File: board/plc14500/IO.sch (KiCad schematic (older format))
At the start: 70 parts, among them U1 74HC14, U2 4051, U3 74HC14, U4 NE555, U5 4099, U6 Arduino Nano

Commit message: Nano board rev-a prod ready
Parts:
- removed R22: 0R, Resistor_THT:R_Axial_DIN0204_L3.6mm_D1.6mm_P7.62mm_Horizontal, symbol Device:R
- D1, D10, D11, D12, D13, D14, D15, D16, D17, D2, D3, D4, D5, D6, D7, D8, D9: value LED 5MM Red -> LED 3MM Red
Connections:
- net +5V: now also U6.27 (+5V)
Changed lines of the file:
@@
 P 7900 2075
 F 0 "D9" H 7925 2150 45  0000 L CNN
-F 1 "LED 5MM Red" H 7978 2036 45  0001 L CNN
+F 1 "LED 3MM Red" H 7978 2036 45  0001 L CNN
 F 2 "plc14500:LED_3MM" V 7700 2075 20  0001 C CNN
 F 3 "" H 7900 2075 50  0001 C CNN
@@
 P 8075 2075
 F 0 "D10" H 8100 2150 45  0000 L CNN
-F 1 "LED 5MM Red" H 8153 2036 45  0001 L CNN
+F 1 "LED 3MM Red" H 8153 2036 45  0001 L CNN
 F 2 "plc14500:LED_3MM" V 7875 2075 20  0001 C CNN
 F 3 "" H 8075 2075 50  0001 C CNN
@@
 P 8250 2075
 F 0 "D11" H 8275 2150 45  0000 L CNN
-F 1 "LED 5MM Red" H 8328 2036 45  0001 L CNN
+F 1 "LED 3MM Red" H 8328 2036 45  0001 L CNN
 F 2 "plc14500:LED_3MM" V 8050 2075 20  0001 C CNN
 F 3 "" H 8250 2075 50  0001 C CNN
@@
 P 8425 2075
 F 0 "D12" H 8450 2150 45  0000 L CNN
-F 1 "LED 5MM Red" H 8503 2036 45  0001 L CNN
+F 1 "LED 3MM Red" H 8503 2036 45  0001 L CNN
 F 2 "plc14500:LED_3MM" V 8225 2075 20  0001 C CNN
 F 3 "" H 8425 2075 50  0001 C CNN
@@
 P 8600 2075
 F 0 "D13" H 8625 2150 45  0000 L CNN
-F 1 "LED 5MM Red" H 8678 2036 45  0001 L CNN
+F 1 "LED 3MM Red" H 8678 2036 45  0001 L CNN
 F 2 "plc14500:LED_3MM" V 8400 2075 20  0001 C CNN
 F 3 "" H 8600 2075 50  0001 C CNN
@@
 P 8775 2075
 F 0 "D14" H 8800 2150 45  0000 L CNN
-F 1 "LED 5MM Red" H 8853 2036 45  0001 L CNN
+F 1 "LED 3MM Red" H 8853 2036 45  0001 L CNN
 F 2 "plc14500:LED_3MM" V 8575 2075 20  0001 C CNN
 F 3 "" H 8775 2075 50  0001 C CNN
@@
 P 8950 2075
 F 0 "D15" H 8975 2150 45  0000 L CNN
-F 1 "LED 5MM Red" H 9028 2036 45  0001 L CNN
+F 1 "LED 3MM Red" H 9028 2036 45  0001 L CNN
 F 2 "plc14500:LED_3MM" V 8750 2075 20  0001 C CNN
 F 3 "" H 8950 2075 50  0001 C CNN
@@
 P 9125 2075
 F 0 "D16" H 9150 2150 45  0000 L CNN
-F 1 "LED 5MM Red" H 9203 2036 45  0001 L CNN
+F 1 "LED 3MM Red" H 9203 2036 45  0001 L CNN
 F 2 "plc14500:LED_3MM" V 8925 2075 20  0001 C CNN
 F 3 "" H 9125 2075 50  0001 C CNN
@@
 P 2250 1875
 F 0 "D1" V 2300 1900 45  0000 L CNN
-F 1 "LED 5MM Red" H 2328 1836 45  0001 L CNN
+F 1 "LED 3MM Red" H 2328 1836 45  0001 L CNN
 F 2 "plc14500:LED_3MM" V 2050 1875 20  0001 C CNN
 F 3 "" H 2250 1875 50  0001 C CNN
@@
 P 6125 6800
 F 0 "D8" H 6150 6875 45  0000 L CNN
-F 1 "LED 5MM Red" H 6203 6761 45  0001 L CNN
+F 1 "LED 3MM Red" H 6203 6761 45  0001 L CNN
 F 2 "plc14500:LED_3MM" V 5925 6800 20  0001 C CNN
 F 3 "" H 6125 6800 50  0001 C CNN
@@
 P 9675 5150
 F 0 "D17" H 9700 5225 45  0000 L CNN
-F 1 "LED 5MM Red" H 9753 5111 45  0001 L CNN
+F 1 "LED 3MM Red" H 9753 5111 45  0001 L CNN
 F 2 "plc14500:LED_3MM" V 9475 5150 20  0001 C CNN
 F 3 "" H 9675 5150 50  0001 C CNN
@@
 P 2250 3500
 F 0 "D2" V 2300 3525 45  0000 L CNN
-F 1 "LED 5MM Red" H 2328 3461 45  0001 L CNN
+F 1 "LED 3MM Red" H 2328 3461 45  0001 L CNN
 F 2 "plc14500:LED_3MM" V 2050 3500 20  0001 C CNN
 F 3 "" H 2250 3500 50  0001 C CNN
@@
 P 2250 4975
 F 0 "D3" V 2300 5000 45  0000 L CNN
-F 1 "LED 5MM Red" H 2328 4936 45  0001 L CNN
+F 1 "LED 3MM Red" H 2328 4936 45  0001 L CNN
 F 2 "plc14500:LED_3MM" V 2050 4975 20  0001 C CNN
 F 3 "" H 2250 4975 50  0001 C CNN
@@
 P 2250 6450
 F 0 "D4" V 2300 6475 45  0000 L CNN
-F 1 "LED 5MM Red" H 2328 6411 45  0001 L CNN
+F 1 "LED 3MM Red" H 2328 6411 45  0001 L CNN
 F 2 "plc14500:LED_3MM" V 2050 6450 20  0001 C CNN
 F 3 "" H 2250 6450 50  0001 C CNN
@@
 P 4775 2025
 F 0 "D5" V 4825 2050 45  0000 L CNN
-F 1 "LED 5MM Red" H 4853 1986 45  0001 L CNN
+F 1 "LED 3MM Red" H 4853 1986 45  0001 L CNN
 F 2 "plc14500:LED_3MM" V 4575 2025 20  0001 C CNN
 F 3 "" H 4775 2025 50  0001 C CNN
@@
 P 4775 3500
 F 0 "D6" V 4825 3525 45  0000 L CNN
-F 1 "LED 5MM Red" H 4853 3461 45  0001 L CNN
+F 1 "LED 3MM Red" H 4853 3461 45  0001 L CNN
 F 2 "plc14500:LED_3MM" V 4575 3500 20  0001 C CNN
 F 3 "" H 4775 3500 50  0001 C CNN
@@
 P 4775 5000
 F 0 "D7" V 4825 5025 45  0000 L CNN
-F 1 "LED 5MM Red" H 4853 4961 45  0001 L CNN
+F 1 "LED 3MM Red" H 4853 4961 45  0001 L CNN
 F 2 "plc14500:LED_3MM" V 4575 5000 20  0001 C CNN
 F 3 "" H 4775 5000 50  0001 C CNN
@@
 Wire Wire Line
 	6900 1400 7075 1400
-$Comp
-L Device:R R22
-U 1 1 68128BF1
-P 8600 3300
-F 0 "R22" V 8700 3300 50  0000 R CNN
-F 1 "0R" V 8500 3300 50  0000 R CNN
-F 2 "Resistor_THT:R_Axial_DIN0204_L3.6mm_D1.6mm_P7.62mm_Horizontal" V 8530 3300 50  0001 C CNN
-F 3 "~" H 8600 3300 50  0001 C CNN
-F 4 "0.01" H 8600 3300 50  0001 C CNN "Price"
-	1    8600 3300
-	0    1    1    0
-$EndComp
 Wire Wire Line
 	8300 3400 8300 3300
-Wire Wire Line
-	8300 3300 8450 3300
-Wire Wire Line
-	8750 3300 8925 3300
 Wire Wire Line
 	8925 3300 8925 3225
@@
 	1    0    0    -1
 $EndComp
+Wire Wire Line
+	8300 3300 8925 3300
 Wire Bus Line
 	6825 1750 6825 2000

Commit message: Update board 3d models
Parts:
- RV1: footprint Potentiometer_THT:Potentiometer_ACP_CA9-H5_Horizontal -> plc14500:HORIZONTAL_POT
- S1, S10, S11, S15, S2, S3, S4, S9: footprint Button_Switch_THT:SW_Tactile_Straight_KSA0Axx1LFTR -> plc14500:SW_Tactile_THT
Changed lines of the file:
@@
 F 0 "S1" V 1075 1500 50  0000 R CNN
 F 1 "Push Button" V 855 1277 50  0001 R CNN
-F 2 "Button_Switch_THT:SW_Tactile_Straight_KSA0Axx1LFTR" H 900 1525 50  0001 C CNN
+F 2 "plc14500:SW_Tactile_THT" H 900 1525 50  0001 C CNN
 F 3 "~" H 900 1525 50  0001 C CNN
 F 4 "0.01" H 900 1325 50  0001 C CNN "Price"
@@
 F 0 "RV1" H 5056 5821 50  0000 R CNN
 F 1 "10K" H 5056 5730 50  0000 R CNN
-F 2 "Potentiometer_THT:Potentiometer_ACP_CA9-H5_Horizontal" H 5125 5775 50  0001 C CNN
+F 2 "plc14500:HORIZONTAL_POT" H 5125 5775 50  0001 C CNN
 F 3 "~" H 5125 5775 50  0001 C CNN
 F 4 "https://www.aliexpress.com/item/1005002935520232.html?spm=a2g0o.productlist.0.0.7a175d89PQda4t&algo_pvid=cfb4e09e-1f4a-43cf-8ff1-6fc20f5cfef2&algo_exp_id=cfb4e09e-1f4a-43cf-8ff1-6fc20f5cfef2-21&pdp_ext_f=%7B%22sku_id%22%3A%2212000022869515902%22%7D&pdp_npi=2%40dis%21EUR%211.49%210.96%21%21%210.35%21%21%400b0a187916678365874186066efa27%2112000022869515902%21sea&curPageLogUid=goQ0aTpXJyrn" H 5125 5775 50  0001 C CNN "Order"
@@
 F 0 "S15" V 9550 4850 50  0000 R CNN
 F 1 "Push Button" V 9330 4627 50  0001 R CNN
-F 2 "Button_Switch_THT:SW_Tactile_Straight_KSA0Axx1LFTR" H 9375 4875 50  0001 C CNN
+F 2 "plc14500:SW_Tactile_THT" H 9375 4875 50  0001 C CNN
 F 3 "~" H 9375 4875 50  0001 C CNN
 F 4 "0.01" H 9375 4675 50  0001 C CNN "Price"
@@
 F 0 "S2" V 1075 3125 50  0000 R CNN
 F 1 "Push Button" V 855 2902 50  0001 R CNN
-F 2 "Button_Switch_THT:SW_Tactile_Straight_KSA0Axx1LFTR" H 900 3150 50  0001 C CNN
+F 2 "plc14500:SW_Tactile_THT" H 900 3150 50  0001 C CNN
 F 3 "~" H 900 3150 50  0001 C CNN
 F 4 "0.01" H 900 2950 50  0001 C CNN "Price"
@@
 F 0 "S3" V 1075 4600 50  0000 R CNN
 F 1 "Push Button" V 855 4377 50  0001 R CNN
-F 2 "Button_Switch_THT:SW_Tactile_Straight_KSA0Axx1LFTR" H 900 4625 50  0001 C CNN
+F 2 "plc14500:SW_Tactile_THT" H 900 4625 50  0001 C CNN
 F 3 "~" H 900 4625 50  0001 C CNN
 F 4 "0.01" H 900 4425 50  0001 C CNN "Price"
@@
 F 0 "S4" V 1075 6075 50  0000 R CNN
 F 1 "Push Button" V 855 5852 50  0001 R CNN
-F 2 "Button_Switch_THT:SW_Tactile_Straight_KSA0Axx1LFTR" H 900 6100 50  0001 C CNN
+F 2 "plc14500:SW_Tactile_THT" H 900 6100 50  0001 C CNN
 F 3 "~" H 900 6100 50  0001 C CNN
 F 4 "0.01" H 900 5900 50  0001 C CNN "Price"
@@
 F 0 "S9" V 3600 1650 50  0000 R CNN
 F 1 "Push Button" V 3380 1427 50  0001 R CNN
-F 2 "Button_Switch_THT:SW_Tactile_Straight_KSA0Axx1LFTR" H 3425 1675 50  0001 C CNN
+F 2 "plc14500:SW_Tactile_THT" H 3425 1675 50  0001 C CNN
 F 3 "~" H 3425 1675 50  0001 C CNN
 F 4 "0.01" H 3425 1475 50  0001 C CNN "Price"
@@
 F 0 "S10" V 3600 3125 50  0000 R CNN
 F 1 "Push Button" V 3380 2902 50  0001 R CNN
-F 2 "Button_Switch_THT:SW_Tactile_Straight_KSA0Axx1LFTR" H 3425 3150 50  0001 C CNN
+F 2 "plc14500:SW_Tactile_THT" H 3425 3150 50  0001 C CNN
 F 3 "~" H 3425 3150 50  0001 C CNN
 F 4 "0.01" H 3425 2950 50  0001 C CNN "Price"
@@
 F 0 "S11" V 3600 4625 50  0000 R CNN
 F 1 "Push Button" V 3380 4402 50  0001 R CNN
-F 2 "Button_Switch_THT:SW_Tactile_Straight_KSA0Axx1LFTR" H 3425 4650 50  0001 C CNN
+F 2 "plc14500:SW_Tactile_THT" H 3425 4650 50  0001 C CNN
 F 3 "~" H 3425 4650 50  0001 C CNN
 F 4 "0.01" H 3425 4450 50  0001 C CNN "Price"

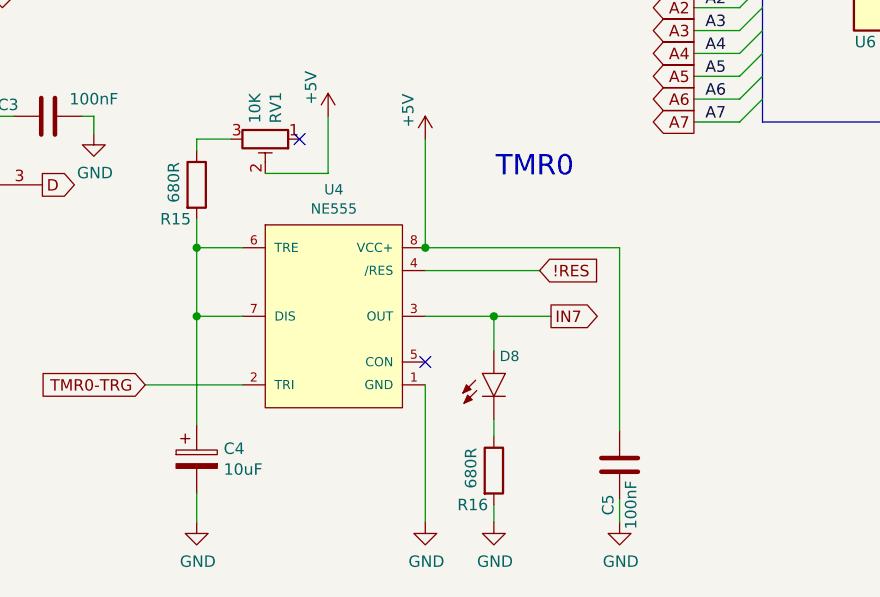
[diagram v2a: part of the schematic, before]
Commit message: Add schematic in PDF format for easier peruse
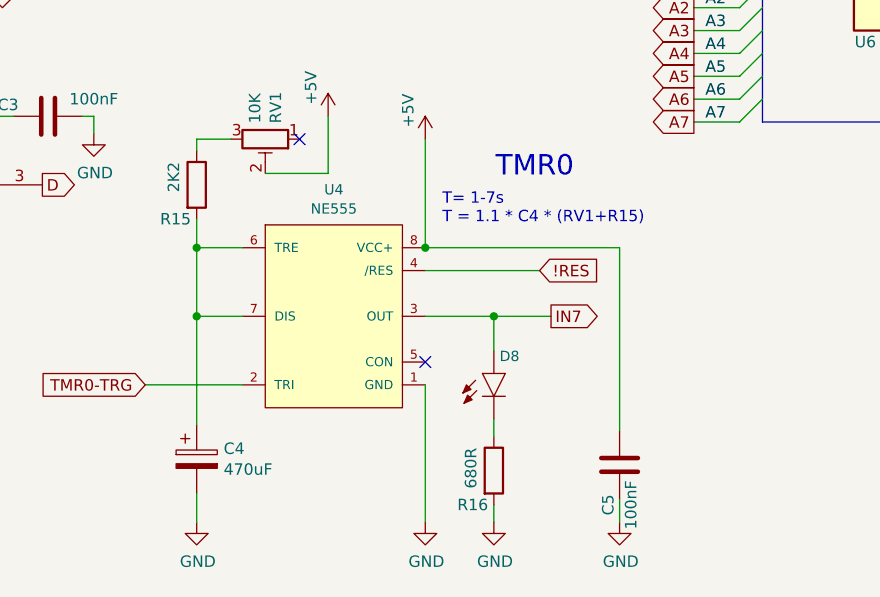
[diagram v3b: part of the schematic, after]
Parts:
- C4: value 10uF -> 470uF
- R15: value 680R -> 2K2
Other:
- note added: "T= 1-7s\nT = 1.1 * C4 * (RV1+R15)"
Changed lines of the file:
@@
 P 4825 5975
 F 0 "R15" H 4800 5825 50  0000 R CNN
-F 1 "680R" V 4725 6075 50  0000 R CNN
+F 1 "2K2" V 4725 6075 50  0000 R CNN
 F 2 "Resistor_THT:R_Axial_DIN0204_L3.6mm_D1.6mm_P7.62mm_Horizontal" V 4755 5975 50  0001 C CNN
 F 3 "~" H 4825 5975 50  0001 C CNN
@@
 AR Path="/63B4BDA9/6376CD92" Ref="C4"  Part="1"
 F 0 "C4" H 4943 7221 50  0000 L CNN
-F 1 "10uF" H 4943 7130 50  0000 L CNN
+F 1 "470uF" H 4943 7130 50  0000 L CNN
 F 2 "Capacitor_THT:CP_Radial_D8.0mm_P5.00mm" H 4863 7025 50  0001 C CNN
 F 3 "~" H 4825 7175 50  0001 C CNN
@@
 Wire Bus Line
 	7300 4700 7300 5700
+Text Notes 5900 6150 0    50   ~ 0
+T= 1-7s\nT = 1.1 * C4 * (RV1+R15)
 $EndSCHEMATC

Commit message: Programmers guide, WIP
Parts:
- added U11: 74HC14, Package_DIP:DIP-14_W7.62mm_LongPads, symbol 74xx:74HC14
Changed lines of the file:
@@
 Text Notes 5900 6150 0    50   ~ 0
 T= 1-7s\nT = 1.1 * C4 * (RV1+R15)
+$Comp
+L 74xx:74HC14 U?
+U 3 1 6389547C
+P 4350 6475
+AR Path="/6389547C" Ref="U?"  Part="1"
+AR Path="/6394A5B3/6389547C" Ref="U?"  Part="2"
+AR Path="/63B4BDA9/6389547C" Ref="U11"  Part="3"
+F 0 "U11" H 4400 6625 50  0000 C CNN
+F 1 "74HC14" H 4200 6275 50  0000 C CNN
+F 2 "Package_DIP:DIP-14_W7.62mm_LongPads" H 4350 6475 50  0001 C CNN
+F 3 "http://www.ti.com/lit/gpn/sn74HC14" H 4350 6475 50  0001 C CNN
+F 4 "0.16" H 4350 6475 50  0001 C CNN "Price"
+	3    4350 6475
+	1    0    0    -1
+$EndComp
 Wire Bus Line
 	6825 1750 6825 2000

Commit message: Rev_b board
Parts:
- added R22: 47K, Resistor_THT:R_Axial_DIN0204_L3.6mm_D1.6mm_P7.62mm_Horizontal, symbol Device:R
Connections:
- net D: now also R22.2; no longer U2.3 (X)
- net TMR0-TRG: now also U11.5; no longer U4.2 (TRI)
- net at U11.6: now also U4.2 (TRI)
- net at R15.1: now also RV1.1; no longer RV1.3
- new net: R22.1, U2.3 (X)
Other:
- moved on the sheet: C4, C5, C6, D10, D11, D12, D13, D14, D15, D16, D17, D8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

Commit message: Updates in preparation for rel 1
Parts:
- R12, R13, R14, R16, R17, R18, R19, R20, R21, R23, R24, R25, R27, R5, R6, R7, R8: value 680R -> 820R
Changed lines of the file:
@@
 P 9300 2475
 F 0 "R17" H 9275 2325 50  0000 R CNN
-F 1 "680R" V 9200 2575 50  0000 R CNN
+F 1 "820R" V 9200 2575 50  0000 R CNN
 F 2 "Resistor_THT:R_Axial_DIN0204_L3.6mm_D1.6mm_P7.62mm_Horizontal" V 9230 2475 50  0001 C CNN
 F 3 "~" H 9300 2475 50  0001 C CNN
@@
 P 9475 2475
 F 0 "R18" H 9450 2325 50  0000 R CNN
-F 1 "680R" V 9375 2575 50  0000 R CNN
+F 1 "820R" V 9375 2575 50  0000 R CNN
 F 2 "Resistor_THT:R_Axial_DIN0204_L3.6mm_D1.6mm_P7.62mm_Horizontal" V 9405 2475 50  0001 C CNN
 F 3 "~" H 9475 2475 50  0001 C CNN
@@
 P 9650 2475
 F 0 "R19" H 9625 2325 50  0000 R CNN
-F 1 "680R" V 9550 2575 50  0000 R CNN
+F 1 "820R" V 9550 2575 50  0000 R CNN
 F 2 "Resistor_THT:R_Axial_DIN0204_L3.6mm_D1.6mm_P7.62mm_Horizontal" V 9580 2475 50  0001 C CNN
 F 3 "~" H 9650 2475 50  0001 C CNN
@@
 P 9825 2475
 F 0 "R20" H 9800 2325 50  0000 R CNN
-F 1 "680R" V 9725 2575 50  0000 R CNN
+F 1 "820R" V 9725 2575 50  0000 R CNN
 F 2 "Resistor_THT:R_Axial_DIN0204_L3.6mm_D1.6mm_P7.62mm_Horizontal" V 9755 2475 50  0001 C CNN
 F 3 "~" H 9825 2475 50  0001 C CNN
@@
 P 10000 2475
 F 0 "R21" H 9975 2325 50  0000 R CNN
-F 1 "680R" V 9900 2575 50  0000 R CNN
+F 1 "820R" V 9900 2575 50  0000 R CNN
 F 2 "Resistor_THT:R_Axial_DIN0204_L3.6mm_D1.6mm_P7.62mm_Horizontal" V 9930 2475 50  0001 C CNN
 F 3 "~" H 10000 2475 50  0001 C CNN
@@
 P 10175 2475
 F 0 "R23" H 10150 2325 50  0000 R CNN
-F 1 "680R" V 10075 2575 50  0000 R CNN
+F 1 "820R" V 10075 2575 50  0000 R CNN
 F 2 "Resistor_THT:R_Axial_DIN0204_L3.6mm_D1.6mm_P7.62mm_Horizontal" V 10105 2475 50  0001 C CNN
 F 3 "~" H 10175 2475 50  0001 C CNN
@@
 P 10350 2475
 F 0 "R24" H 10325 2325 50  0000 R CNN
-F 1 "680R" V 10250 2575 50  0000 R CNN
+F 1 "820R" V 10250 2575 50  0000 R CNN
 F 2 "Resistor_THT:R_Axial_DIN0204_L3.6mm_D1.6mm_P7.62mm_Horizontal" V 10280 2475 50  0001 C CNN
 F 3 "~" H 10350 2475 50  0001 C CNN
@@
 P 10525 2475
 F 0 "R25" H 10500 2325 50  0000 R CNN
-F 1 "680R" V 10425 2575 50  0000 R CNN
+F 1 "820R" V 10425 2575 50  0000 R CNN
 F 2 "Resistor_THT:R_Axial_DIN0204_L3.6mm_D1.6mm_P7.62mm_Horizontal" V 10455 2475 50  0001 C CNN
 F 3 "~" H 10525 2475 50  0001 C CNN
@@
 P 1775 1875
 F 0 "R5" V 1875 1925 50  0000 R CNN
-F 1 "680R" V 1675 1975 50  0000 R CNN
+F 1 "820R" V 1675 1975 50  0000 R CNN
 F 2 "Resistor_THT:R_Axial_DIN0204_L3.6mm_D1.6mm_P7.62mm_Horizontal" V 1705 1875 50  0001 C CNN
 F 3 "~" H 1775 1875 50  0001 C CNN
@@
 P 7800 6100
 F 0 "R16" H 7775 5950 50  0000 R CNN
-F 1 "680R" V 7700 6200 50  0000 R CNN
+F 1 "820R" V 7700 6200 50  0000 R CNN
 F 2 "Resistor_THT:R_Axial_DIN0204_L3.6mm_D1.6mm_P7.62mm_Horizontal" V 7730 6100 50  0001 C CNN
 F 3 "~" H 7800 6100 50  0001 C CNN
@@
 P 8800 4175
 F 0 "R27" H 8775 4025 50  0000 R CNN
-F 1 "680R" V 8700 4275 50  0000 R CNN
+F 1 "820R" V 8700 4275 50  0000 R CNN
 F 2 "Resistor_THT:R_Axial_DIN0204_L3.6mm_D1.6mm_P7.62mm_Horizontal" V 8730 4175 50  0001 C CNN
 F 3 "~" H 8800 4175 50  0001 C CNN
@@
 P 1775 3500
 F 0 "R6" V 1875 3550 50  0000 R CNN
-F 1 "680R" V 1675 3600 50  0000 R CNN
+F 1 "820R" V 1675 3600 50  0000 R CNN
 F 2 "Resistor_THT:R_Axial_DIN0204_L3.6mm_D1.6mm_P7.62mm_Horizontal" V 1705 3500 50  0001 C CNN
 F 3 "~" H 1775 3500 50  0001 C CNN
@@
 P 1775 4975
 F 0 "R7" V 1875 5025 50  0000 R CNN
-F 1 "680R" V 1675 5075 50  0000 R CNN
+F 1 "820R" V 1675 5075 50  0000 R CNN
 F 2 "Resistor_THT:R_Axial_DIN0204_L3.6mm_D1.6mm_P7.62mm_Horizontal" V 1705 4975 50  0001 C CNN
 F 3 "~" H 1775 4975 50  0001 C CNN
@@
 P 1775 6450
 F 0 "R8" V 1875 6500 50  0000 R CNN
-F 1 "680R" V 1675 6550 50  0000 R CNN
+F 1 "820R" V 1675 6550 50  0000 R CNN
 F 2 "Resistor_THT:R_Axial_DIN0204_L3.6mm_D1.6mm_P7.62mm_Horizontal" V 1705 6450 50  0001 C CNN
 F 3 "~" H 1775 6450 50  0001 C CNN
@@
 P 4300 2025
 F 0 "R12" V 4400 2075 50  0000 R CNN
-F 1 "680R" V 4200 2125 50  0000 R CNN
+F 1 "820R" V 4200 2125 50  0000 R CNN
 F 2 "Resistor_THT:R_Axial_DIN0204_L3.6mm_D1.6mm_P7.62mm_Horizontal" V 4230 2025 50  0001 C CNN
 F 3 "~" H 4300 2025 50  0001 C CNN
@@
 P 4300 3500
 F 0 "R13" V 4400 3550 50  0000 R CNN
-F 1 "680R" V 4200 3600 50  0000 R CNN
+F 1 "820R" V 4200 3600 50  0000 R CNN
 F 2 "Resistor_THT:R_Axial_DIN0204_L3.6mm_D1.6mm_P7.62mm_Horizontal" V 4230 3500 50  0001 C CNN
 F 3 "~" H 4300 3500 50  0001 C CNN
@@
 P 4300 5000
 F 0 "R14" V 4400 5050 50  0000 R CNN
-F 1 "680R" V 4200 5100 50  0000 R CNN
+F 1 "820R" V 4200 5100 50  0000 R CNN
 F 2 "Resistor_THT:R_Axial_DIN0204_L3.6mm_D1.6mm_P7.62mm_Horizontal" V 4230 5000 50  0001 C CNN
 F 3 "~" H 4300 5000 50  0001 C CNN

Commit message: Rescue some missing symbols that were broken
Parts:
- D1, D10, D11, D12, D13, D14, D15, D16, D17, D2, D3, D4, D5, D6, D7, D8, D9: symbol SparkFun-LED:LED5MM -> plc14500-rescue:LED5MM-SparkFun-LED
- S12, S13, S14, S5, S6, S7, S8: symbol SparkFun-Switches:SWITCH-DPDT-PTH-GPI-152-3013 -> plc14500-rescue:SWITCH-DPDT-PTH-GPI-152-3013-SparkFun-Switches
- U4: symbol SparkFun-IC-Special-Function:555D -> plc14500-rescue:555D-SparkFun-IC-Special-Function
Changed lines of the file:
@@
 $EndDescr
 $Comp
-L SparkFun-LED:LED5MM D9
+L plc14500-rescue:LED5MM-SparkFun-LED D9
 U 1 1 63B7B5F6
 P 9300 2025
@@
 $EndComp
 $Comp
-L SparkFun-LED:LED5MM D10
+L plc14500-rescue:LED5MM-SparkFun-LED D10
 U 1 1 63B7B5FD
 P 9475 2025
@@
 $EndComp
 $Comp
-L SparkFun-LED:LED5MM D11
+L plc14500-rescue:LED5MM-SparkFun-LED D11
 U 1 1 63B7B604
 P 9650 2025
@@
 $EndComp
 $Comp
-L SparkFun-LED:LED5MM D12
+L plc14500-rescue:LED5MM-SparkFun-LED D12
 U 1 1 63B7B60B
 P 9825 2025
@@
 $EndComp
 $Comp
-L SparkFun-LED:LED5MM D13
+L plc14500-rescue:LED5MM-SparkFun-LED D13
 U 1 1 63B7B612
 P 10000 2025
@@
 $EndComp
 $Comp
-L SparkFun-LED:LED5MM D14
+L plc14500-rescue:LED5MM-SparkFun-LED D14
 U 1 1 63B7B619
 P 10175 2025
@@
 $EndComp
 $Comp
-L SparkFun-LED:LED5MM D15
+L plc14500-rescue:LED5MM-SparkFun-LED D15
 U 1 1 63B7B620
 P 10350 2025
@@
 	10350 1250 10350 1925
 $Comp
-L SparkFun-LED:LED5MM D16
+L plc14500-rescue:LED5MM-SparkFun-LED D16
 U 1 1 6364A55C
 P 10525 2025
@@
 	8425 900  8425 775
 $Comp
-L SparkFun-Switches:SWITCH-DPDT-PTH-GPI-152-3013 S?
+L plc14500-rescue:SWITCH-DPDT-PTH-GPI-152-3013-SparkFun-Switches S?
 U 1 1 63712537
 P 1275 1325
@@
 	1475 1425 1600 1425
 $Comp
-L SparkFun-LED:LED5MM D1
+L plc14500-rescue:LED5MM-SparkFun-LED D1
 U 1 1 6373C762
 P 2250 1875
@@
 	8875 2125 8875 2100
 $Comp
-L SparkFun-IC-Special-Function:555D U?
+L plc14500-rescue:555D-SparkFun-IC-Special-Function U?
 U 1 1 65241B0B
 P 7100 5475
@@
 	7500 5275 8000 5275
 $Comp
-L SparkFun-LED:LED5MM D8
+L plc14500-rescue:LED5MM-SparkFun-LED D8
 U 1 1 655C29A5
 P 7800 5725
@@
 $EndComp
 $Comp
-L SparkFun-LED:LED5MM D17
+L plc14500-rescue:LED5MM-SparkFun-LED D17
 U 1 1 6458A3D8
 P 8800 3775
@@
 Connection ~ 2450 900
 $Comp
-L SparkFun-Switches:SWITCH-DPDT-PTH-GPI-152-3013 S?
+L plc14500-rescue:SWITCH-DPDT-PTH-GPI-152-3013-SparkFun-Switches S?
 U 1 1 67F00B9F
 P 1275 2950
@@
 	1475 3050 1600 3050
 $Comp
-L SparkFun-LED:LED5MM D2
+L plc14500-rescue:LED5MM-SparkFun-LED D2
 U 1 1 67F00BC1
 P 2250 3500
@@
 Connection ~ 2450 2525
 $Comp
-L SparkFun-Switches:SWITCH-DPDT-PTH-GPI-152-3013 S?
+L plc14500-rescue:SWITCH-DPDT-PTH-GPI-152-3013-SparkFun-Switches S?
 U 1 1 67F0FC99
 P 1275 4425
@@
 	1475 4525 1600 4525
 $Comp
-L SparkFun-LED:LED5MM D3
+L plc14500-rescue:LED5MM-SparkFun-LED D3
 U 1 1 67F0FCBB
 P 2250 4975
@@
 Connection ~ 2450 4000
 $Comp
-L SparkFun-Switches:SWITCH-DPDT-PTH-GPI-152-3013 S?
+L plc14500-rescue:SWITCH-DPDT-PTH-GPI-152-3013-SparkFun-Switches S?
 U 1 1 67F20B47
 P 1275 5900
@@
 	1475 6000 1600 6000
 $Comp
-L SparkFun-LED:LED5MM D4
+L plc14500-rescue:LED5MM-SparkFun-LED D4
 U 1 1 67F20B69
 P 2250 6450
@@
 Connection ~ 2450 5475
 $Comp
-L SparkFun-Switches:SWITCH-DPDT-PTH-GPI-152-3013 S?
+L plc14500-rescue:SWITCH-DPDT-PTH-GPI-152-3013-SparkFun-Switches S?
 U 1 1 67F36733
 P 3800 1475
@@
 	4000 1575 4125 1575
 $Comp
-L SparkFun-LED:LED5MM D5
+L plc14500-rescue:LED5MM-SparkFun-LED D5
 U 1 1 67F36755
 P 4775 2025
@@
 Connection ~ 4975 1050
 $Comp
-L SparkFun-Switches:SWITCH-DPDT-PTH-GPI-152-3013 S?
+L plc14500-rescue:SWITCH-DPDT-PTH-GPI-152-3013-SparkFun-Switches S?
 U 1 1 67F4EAB0
 P 3800 2950
@@
 	4000 3050 4125 3050
 $Comp
-L SparkFun-LED:LED5MM D6
+L plc14500-rescue:LED5MM-SparkFun-LED D6
 U 1 1 67F4EAD2
 P 4775 3500
@@
 Connection ~ 4975 2525
 $Comp
-L SparkFun-Switches:SWITCH-DPDT-PTH-GPI-152-3013 S?
+L plc14500-rescue:SWITCH-DPDT-PTH-GPI-152-3013-SparkFun-Switches S?
 U 1 1 67F6A3FB
 P 3800 4450
@@
 	4000 4550 4125 4550
 $Comp
-L SparkFun-LED:LED5MM D7
+L plc14500-rescue:LED5MM-SparkFun-LED D7
 U 1 1 67F6A41D
 P 4775 5000
